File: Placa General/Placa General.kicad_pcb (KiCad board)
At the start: 2 copper layers, 26 parts

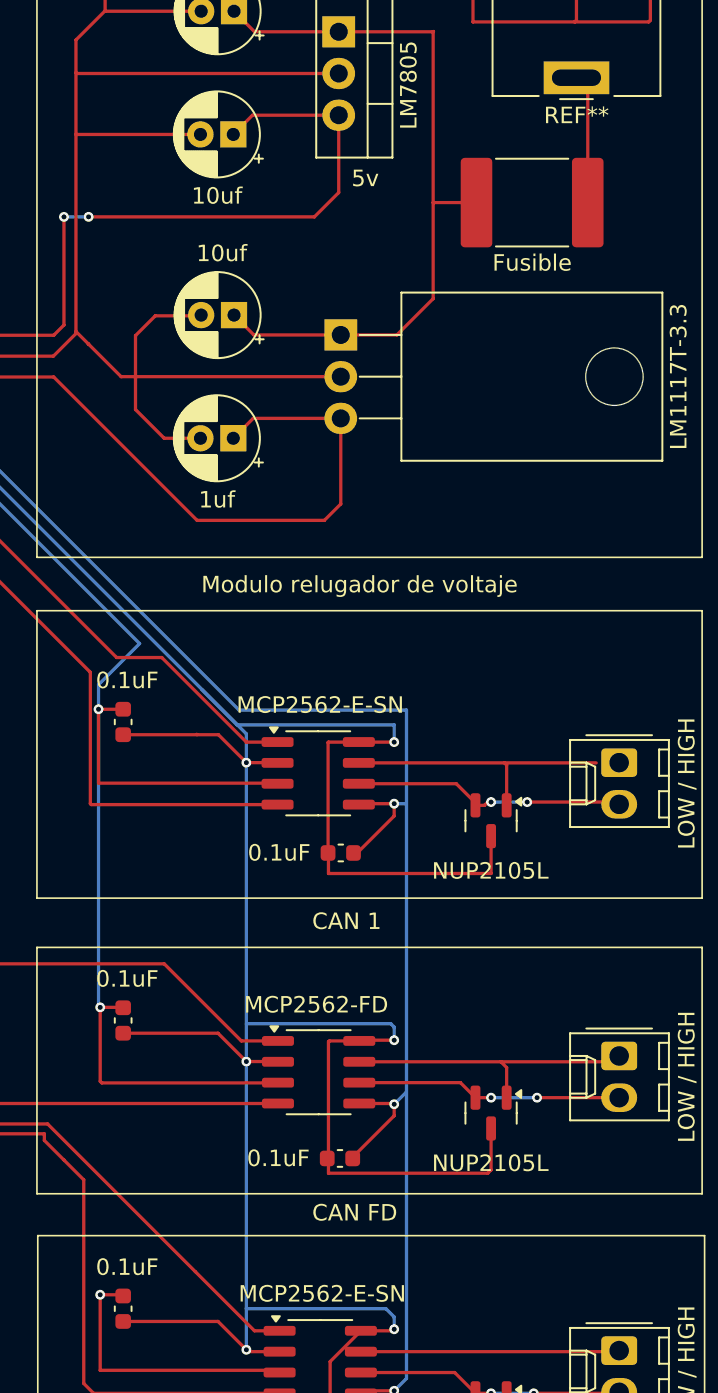
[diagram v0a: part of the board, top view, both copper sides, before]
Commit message: Error Placa
Tenia un error, en los pines de voltajes del can 2, y no tenia referencias en el conector de 12v
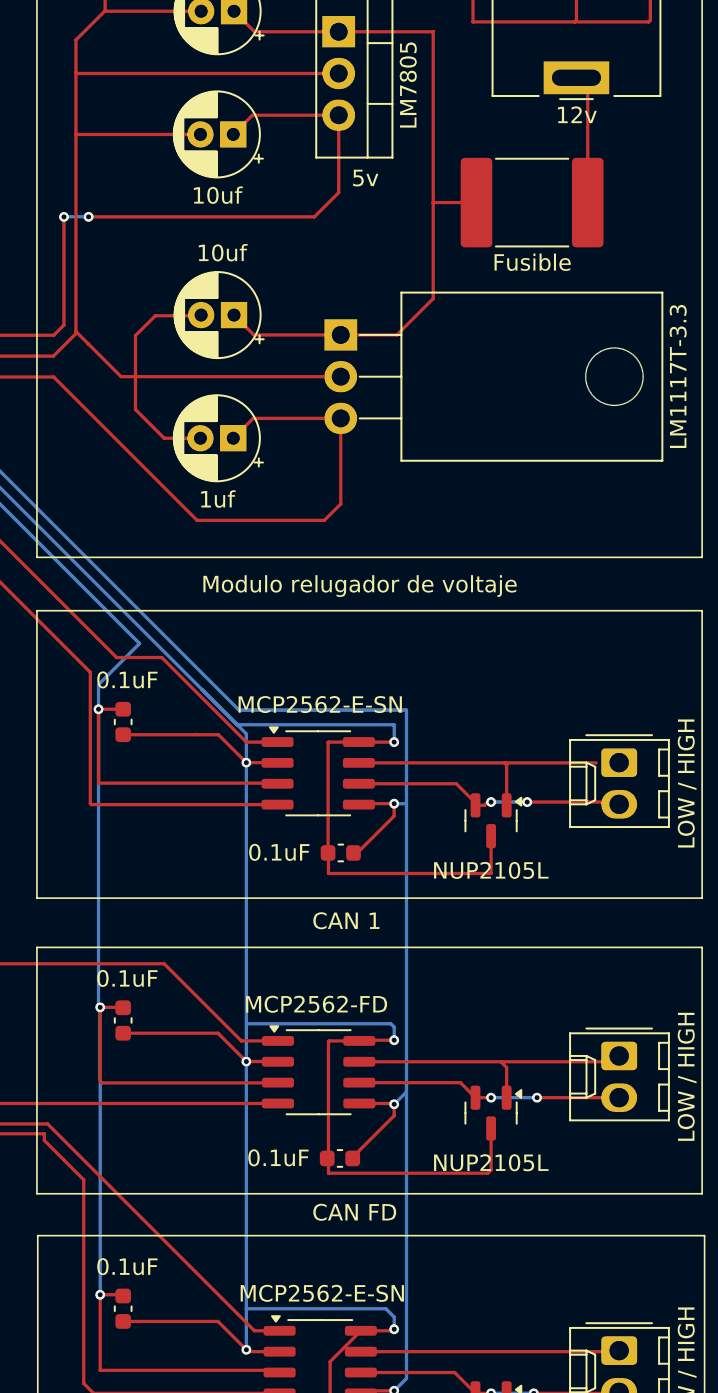
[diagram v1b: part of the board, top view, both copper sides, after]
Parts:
- renumbered REF** to 12v
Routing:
- net unconnected-(U1-VDD-Pad3): track 365.4 -> 399.8 mm, vias 8 -> 9
- net (no net): track 580.9 -> 563.8 mm, vias 11 -> 10
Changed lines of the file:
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@@
 		(tags "capacitor")
 		(property "Reference" "0.1uF"
-			(at -3.75 0 360)
+			(at -3.75 0 0)
 			(layer "F.SilkS")
 			(effects
@@
 		)
 		(property "Value" "C_0603_1608Metric"
-			(at 0 1.43 360)
+			(at 0 1.43 0)
 			(layer "F.Fab")
 			(hide yes)
@@
 		)
 		(fp_text user "${REFERENCE}"
-			(at 0 0 360)
+			(at 0 0 0)
 			(layer "F.Fab")
 			(effects
@@
 		(descr "Barrel Jack, 2.0mm ID, 5.5mm OD, 24V, 8A, no switch, https://www.cui.com/product/resource/pj-063ah.pdf")
 		(tags "barrel jack cui dc power")
-		(property "Reference" "REF**"
+		(property "Reference" "12v"
 			(at 0 -2.3 180)
 			(layer "F.SilkS")
@@
 	)
 	(segment
-		(start 156.39 117)
-		(end 156.525 117.135)
-		(width 0.2)
-		(layer "F.Cu")
-		(net 0)
-	)
-	(segment
 		(start 103.8 85.4)
 		(end 103.8 84.6)
@@
 	)
 	(segment
-		(start 145.6 112.4)
-		(end 145.6 117)
-		(width 0.2)
-		(layer "F.Cu")
-		(net 0)
-	)
-	(segment
 		(start 120.4 102)
 		(end 103.8 85.4)
@@
 	)
 	(segment
-		(start 145.6 112.4)
-		(end 146.925 112.4)
-		(width 0.2)
-		(layer "F.Cu")
-		(net 0)
-	)
-	(segment
-		(start 145.6 117)
-		(end 156.39 117)
-		(width 0.2)
-		(layer "F.Cu")
-		(net 0)
-	)
-	(segment
 		(start 161.42 96.9)
 		(end 161.375 96.945)
@@
 	)
 	(segment
-		(start 146.925 112.4)
-		(end 147 112.475)
-		(width 0.2)
-		(layer "F.Cu")
-		(net 0)
-	)
-	(segment
 		(start 159.5 97)
 		(end 159.5 104.025)
@@
 	)
 	(via
-		(at 145.6 112.4)
-		(size 0.6)
-		(drill 0.3)
-		(layers "F.Cu" "B.Cu")
-		(net 0)
-	)
-	(via
 		(at 169.4 82.4)
 		(size 0.6)
@@
 	)
 	(segment
+		(start 156.39 117)
+		(end 156.525 117.135)
+		(width 0.2)
+		(layer "F.Cu")
+		(net 8)
+	)
+	(segment
 		(start 144.125 53.875)
 		(end 142.75 55.25)
@@
 	)
 	(segment
+		(start 145.6 112.4)
+		(end 145.6 117)
+		(width 0.2)
+		(layer "F.Cu")
+		(net 8)
+	)
+	(segment
 		(start 147.75 54)
 		(end 148.955113 52.794887)
@@
 	)
 	(segment
+		(start 145.6 112.4)
+		(end 146.925 112.4)
+		(width 0.2)
+		(layer "F.Cu")
+		(net 8)
+	)
+	(segment
+		(start 145.6 117)
+		(end 156.39 117)
+		(width 0.2)
+		(layer "F.Cu")
+		(net 8)
+	)
+	(segment
 		(start 162.1 78.75)
 		(end 162 78.65)
@@
 	)
 	(segment
+		(start 146.925 112.4)
+		(end 147 112.475)
+		(width 0.2)
+		(layer "F.Cu")
+		(net 8)
+	)
+	(segment
 		(start 144.125 38)
 		(end 144.125 53.875)
@@
 		(net 8)
 	)
+	(via
+		(at 145.6 112.4)
+		(size 0.6)
+		(drill 0.3)
+		(layers "F.Cu" "B.Cu")
+		(net 8)
+	)
 	(segment
 		(start 145.5 75.25)
@@
 		(width 0.2)
 		(layer "B.Cu")
+		(net 8)
+	)
+	(segment
+		(start 145.6 94.9)
+		(end 145.6 112.3)
+		(width 0.2)
+		(layer "B.Cu")
